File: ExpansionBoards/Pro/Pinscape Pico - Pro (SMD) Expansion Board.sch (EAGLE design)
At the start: 175 parts, among them IC1 UCC27523D, IC10 UCC27523D, IC11 UCC27523D, IC12 UCC27523D, IC13 UCC27523D, IC14 UCC27523D, IC15 TLC59116FIRHBR, IC16 TLC59116FIRHBR, IC17 TLC59116FIRHBR, IC18 TLC59116FIRHBR, IC19 ULN2803ADWR, IC2 UCC27523D, IC20 ULN2803ADWR, IC21 ULN2803ADWR, IC22 ULN2803ADWR, IC23 ULN2803ADWR, IC24 PCA9555APW,118, IC25 PCA9555APW,118, IC26 LIS3DHTR, IC27 SN74LVC1G175DCKR, IC28 APX809S-29SA-7, IC29 LTV-827S, IC3 UCC27523D, IC30 ADS1115IDGSR, IC31 TLV75733PDBVR, IC33 RV-3032-C7, IC4 UCC27523D, IC5 UCC27523D, IC6 UCC27523D, IC7 UCC27523D, IC8 UCC27523D, IC9 UCC27523D, J1 640445-4, J10 1-640456-0, J11 1-640456-0, J12 1-640456-0, J13 640445-5, J14 640445-9, J15 640445-9, J16 640445-9, J18 BM03B-SRSS-TB(LF)(SN), J2 30316-6002HB, J3 1-640456-0, J4 640456-9, J5 640456-9, J6 640454-2, J7 215079-4, J8 30308-6002HB, J9 1-640456-0, Q1 BUK7K89-100EX, Q10 BUK7K89-100EX, Q11 BUK7K89-100EX, Q12 BUK7K89-100EX, Q13 BUK7K89-100EX, Q14 BUK7K89-100EX, Q15 UMA5NTR, Q16 UMA5NTR, Q17 UMA5NTR, Q18 UMA5NTR, Q19 UMA5NTR, Q2 BUK7K89-100EX, Q20 UMA5NTR, Q21 UMA5NTR, Q22 UMA5NTR, Q23 UMA5NTR, Q24 UMA5NTR, Q25 UMA5NTR, Q26 UMA5NTR, Q29 DMG2302UK-7, Q3 BUK7K89-100EX, Q4 BUK7K89-100EX, Q5 BUK7K89-100EX, Q6 BUK7K89-100EX, Q7 BUK7K89-100EX, Q8 BUK7K89-100EX, Q9 BUK7K89-100EX, SW1 TS-1187A-B-A-B, U1 BAT-HLD-001-THM

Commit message: bug fixes
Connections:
- net 3V3_PERIPHERAL: now also IC26.CS
- net GND: now also IC26.SDO/SA0; no longer IC26.CS
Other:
- note added: "CS = VDD -> I2C mode"
- note added: "I2C Addresses Use 7-bit address notation, per Pico SDK conventions $18 LIS3DHTR (accelerometer) $20 IC24 PCA9555 (GPIO expander) $21 IC25 PCA9555 (GPIO expander) $48 IC29 ADS1115 (ADC) $51 IC32 RV-3032-C7 (RTC) $60 IC15 TLC59116F (PWM) $61 IC16 TLC59116F (PWM) $62 IC17 TLC59116F (PWM) $63 IC18 TLC59116F (PWM) Note: TLC59116F addresses $68 and $6B are reserved; do not use for new chips added to th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"
- note added: "SDO/SA0 sets I2C address: GND = 0x18, VDD = 0x19"
- note removed: "I2C Addresses Use 7-bit address notation, per Pico SDK conventions $20 IC24 PCA9555 (GPIO expander) $21 IC25 PCA9555 (GPIO expander) $48 IC29 ADS1115 (ADC) $4C IC15 MC3416 (Accelerometer) $51 IC32 RV-3032-C7 (RTC) $60 IC15 TLC59116F (PWM) $61 IC16 TLC59116F (PWM) $62 IC17 TLC59116F (PWM) $63 IC18 TLC59116F (PWM) Note: TLC59116F addresses $68 and $6B are reserved; do not use for new chips added to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"
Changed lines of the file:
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@@
 <part name="J19" library="pinhead" deviceset="PINHD-1X6" device=""/>
 <part name="IC26" library="SamacSys_Parts" deviceset="LIS3DHTR" device=""/>
-<part name="GND42" library="supply1" deviceset="GND" device=""/>
 <part name="GND51" library="supply1" deviceset="GND" device=""/>
 <part name="GND52" library="supply1" deviceset="GND" device=""/>
@@
 <part name="R49" library="resistor" deviceset="R-US_" device="R0402" value="100R"/>
 <part name="R50" library="resistor" deviceset="R-US_" device="R0402" value="330R"/>
+<part name="GND42" library="supply1" deviceset="GND" device=""/>
 </parts>
 <sheets>
@@
 <plain>
 <text x="73.66" y="68.58" size="2.54" layer="91">Accelerometer</text>
+<text x="81.28" y="-3.048" size="1.778" layer="91" align="center-left">SDO/SA0 sets I2C address:
+GND = 0x18, VDD = 0x19</text>
+<text x="107.95" y="7.874" size="1.778" layer="91" align="center-left">CS = VDD -&gt; I2C mode</text>
 </plain>
 <instances>
@@
 <attribute name="VALUE" x="97.79" y="22.86" size="1.778" layer="96" align="center-left"/>
 </instance>
-<instance part="GND42" gate="1" x="86.36" y="5.08" rot="MR0"/>
 <instance part="GND51" gate="1" x="60.96" y="35.56" rot="MR90"/>
 <instance part="GND52" gate="1" x="106.68" y="38.1" rot="MR270"/>
 <instance part="GND50" gate="1" x="106.68" y="43.18" rot="MR270"/>
+<instance part="GND42" gate="1" x="83.82" y="2.54" rot="MR0"/>
 </instances>
 <busses>
@@
 </segment>
 <segment>
-<pinref part="IC26" gate="G$1" pin="CS"/>
-<pinref part="GND42" gate="1" pin="GND"/>
-<wire x1="86.36" y1="10.16" x2="86.36" y2="7.62" width="0.1524" layer="91"/>
-</segment>
-<segment>
 <pinref part="GND51" gate="1" pin="GND"/>
 <pinref part="IC26" gate="G$1" pin="GND_1"/>
@@
 <pinref part="GND50" gate="1" pin="GND"/>
 </segment>
+<segment>
+<pinref part="IC26" gate="G$1" pin="SDO/SA0"/>
+<wire x1="83.82" y1="10.16" x2="83.82" y2="5.08" width="0.1524" layer="91"/>
+<pinref part="GND42" gate="1" pin="GND"/>
+</segment>
 </net>
 <net name="SDA" class="0">
@@
 <pinref part="IC26" gate="G$1" pin="SDA/SDI/SDO"/>
 <wire x1="81.28" y1="10.16" x2="81.28" y2="7.62" width="0.1524" layer="91"/>
-<label x="81.28" y="7.62" size="1.27" layer="95" rot="R270" xref="yes"/>
+<wire x1="81.28" y1="7.62" x2="78.74" y2="7.62" width="0.1524" layer="91"/>
+<label x="78.74" y="7.62" size="1.27" layer="95" rot="R180" xref="yes"/>
 </segment>
 </net>
@@
 <junction x="43.18" y="45.72"/>
 </segment>
+<segment>
+<wire x1="88.9" y1="7.62" x2="86.36" y2="7.62" width="0.1524" layer="91"/>
+<pinref part="IC26" gate="G$1" pin="CS"/>
+<wire x1="86.36" y1="7.62" x2="86.36" y2="10.16" width="0.1524" layer="91"/>
+<label x="88.9" y="7.62" size="1.27" layer="95" xref="yes"/>
+</segment>
 </net>
 </nets>
@@
 Use 7-bit address notation, per
 Pico SDK conventions
+  $18  LIS3DHTR (accelerometer)
   $20  IC24 PCA9555 (GPIO expander)
   $21  IC25 PCA9555 (GPIO expander)
   $48  IC29 ADS1115 (ADC)
-  $4C  IC15 MC3416 (Accelerometer)
   $51  IC32 RV-3032-C7 (RTC)
   $60  IC15 TLC59116F (PWM)

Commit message: expansion board improvements
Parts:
- J1: value 640445-4 -> 640445-6; device SamacSys_Parts:640445-4 -> SamacSys_Parts:640445-6
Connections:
- net 12V: now also J1.5; no longer J1.4
- net 5V: now also J1.6; no longer J1.1
- net GND: now also J1.1, J1.4
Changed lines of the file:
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@@
 <part name="J11" library="SamacSys_Parts" deviceset="1-640456-0" device=""/>
 <part name="J12" library="SamacSys_Parts" deviceset="1-640456-0" device=""/>
-<part name="J1" library="SamacSys_Parts" deviceset="640445-4" device=""/>
 <part name="J7" library="SamacSys_Parts" deviceset="215079-4" device=""/>
 <part name="GND7" library="supply1" deviceset="GND" device=""/>
@@
 <part name="R50" library="resistor" deviceset="R-US_" device="R0402" value="330R"/>
 <part name="GND42" library="supply1" deviceset="GND" device=""/>
+<part name="J1" library="SamacSys_Parts" deviceset="640445-6" device=""/>
 </parts>
 <sheets>
@@
 <attribute name="NAME" x="99.06" y="78.74" size="2.54" layer="95" align="center"/>
 </instance>
-<instance part="GND1" gate="1" x="25.4" y="119.38" rot="R270"/>
+<instance part="GND1" gate="1" x="38.1" y="121.92" rot="R270"/>
 <instance part="R41" gate="G$1" x="205.74" y="50.8" smashed="yes" rot="R90">
 <attribute name="NAME" x="207.264" y="51.2826" size="1.778" layer="95"/>
@@
 <attribute name="NAME" x="104.648" y="121.3866" size="1.778" layer="95"/>
 <attribute name="VALUE" x="110.49" y="121.412" size="1.778" layer="96"/>
-</instance>
-<instance part="J1" gate="G$1" x="45.72" y="121.92" smashed="yes">
-<attribute name="NAME" x="61.722" y="122.936" size="1.778" layer="95" align="center-left"/>
-<attribute name="VALUE" x="61.722" y="120.396" size="1.778" layer="96" align="center-left"/>
 </instance>
 <instance part="J18" gate="A" x="208.28" y="116.84" smashed="yes">
@@
 </instance>
 <instance part="GND49" gate="1" x="314.96" y="12.7"/>
+<instance part="J1" gate="G$1" x="45.72" y="121.92" smashed="yes">
+<attribute name="NAME" x="62.23" y="121.92" size="1.778" layer="95" align="center-left"/>
+<attribute name="VALUE" x="62.23" y="119.38" size="1.778" layer="96" align="center-left"/>
+</instance>
 </instances>
 <busses>
@@
 <net name="GND" class="0">
 <segment>
-<wire x1="45.72" y1="119.38" x2="30.48" y2="119.38" width="0.1524" layer="91"/>
-<wire x1="45.72" y1="116.84" x2="30.48" y2="116.84" width="0.1524" layer="91"/>
-<wire x1="30.48" y1="116.84" x2="30.48" y2="119.38" width="0.1524" layer="91"/>
-<wire x1="30.48" y1="119.38" x2="27.94" y2="119.38" width="0.1524" layer="91"/>
+<wire x1="45.72" y1="116.84" x2="43.18" y2="116.84" width="0.1524" layer="91"/>
+<wire x1="43.18" y1="116.84" x2="43.18" y2="119.38" width="0.1524" layer="91"/>
+<wire x1="43.18" y1="119.38" x2="43.18" y2="121.92" width="0.1524" layer="91"/>
+<wire x1="43.18" y1="121.92" x2="40.64" y2="121.92" width="0.1524" layer="91"/>
 <pinref part="GND1" gate="1" pin="GND"/>
-<junction x="30.48" y="119.38"/>
+<junction x="43.18" y="121.92"/>
+<wire x1="43.18" y1="116.84" x2="43.18" y2="114.3" width="0.1524" layer="91"/>
+<junction x="43.18" y="116.84"/>
+<wire x1="43.18" y1="114.3" x2="45.72" y2="114.3" width="0.1524" layer="91"/>
 <pinref part="J1" gate="G$1" pin="2"/>
 <pinref part="J1" gate="G$1" pin="3"/>
+<pinref part="J1" gate="G$1" pin="4"/>
+<wire x1="45.72" y1="119.38" x2="43.18" y2="119.38" width="0.1524" layer="91"/>
+<junction x="43.18" y="119.38"/>
+<pinref part="J1" gate="G$1" pin="1"/>
+<wire x1="43.18" y1="121.92" x2="45.72" y2="121.92" width="0.1524" layer="91"/>
 </segment>
 <segment>
@@
 <net name="5V" class="0">
 <segment>
-<label x="43.18" y="121.92" size="1.27" layer="95" rot="R180" xref="yes"/>
-<pinref part="J1" gate="G$1" pin="1"/>
-<wire x1="43.18" y1="121.92" x2="45.72" y2="121.92" width="0.1524" layer="91"/>
+<label x="43.18" y="109.22" size="1.27" layer="95" rot="R180" xref="yes"/>
+<pinref part="J1" gate="G$1" pin="6"/>
+<wire x1="45.72" y1="109.22" x2="43.18" y2="109.22" width="0.1524" layer="91"/>
 </segment>
 </net>
@@
 <net name="12V" class="0">
 <segment>
-<label x="43.18" y="114.3" size="1.27" layer="95" rot="R180" xref="yes"/>
-<pinref part="J1" gate="G$1" pin="4"/>
-<wire x1="43.18" y1="114.3" x2="45.72" y2="114.3" width="0.1524" layer="91"/>
-</segment>
-</net>
+<label x="43.18" y="111.76" size="1.27" layer="95" rot="R180" xref="yes"/>
+<pinref part="J1" gate="G$1" pin="5"/>
+<wire x1="45.72" y1="111.76" x2="43.18" y2="111.76" width="0.1524" layer="91"/>
+</segment>
+</net>

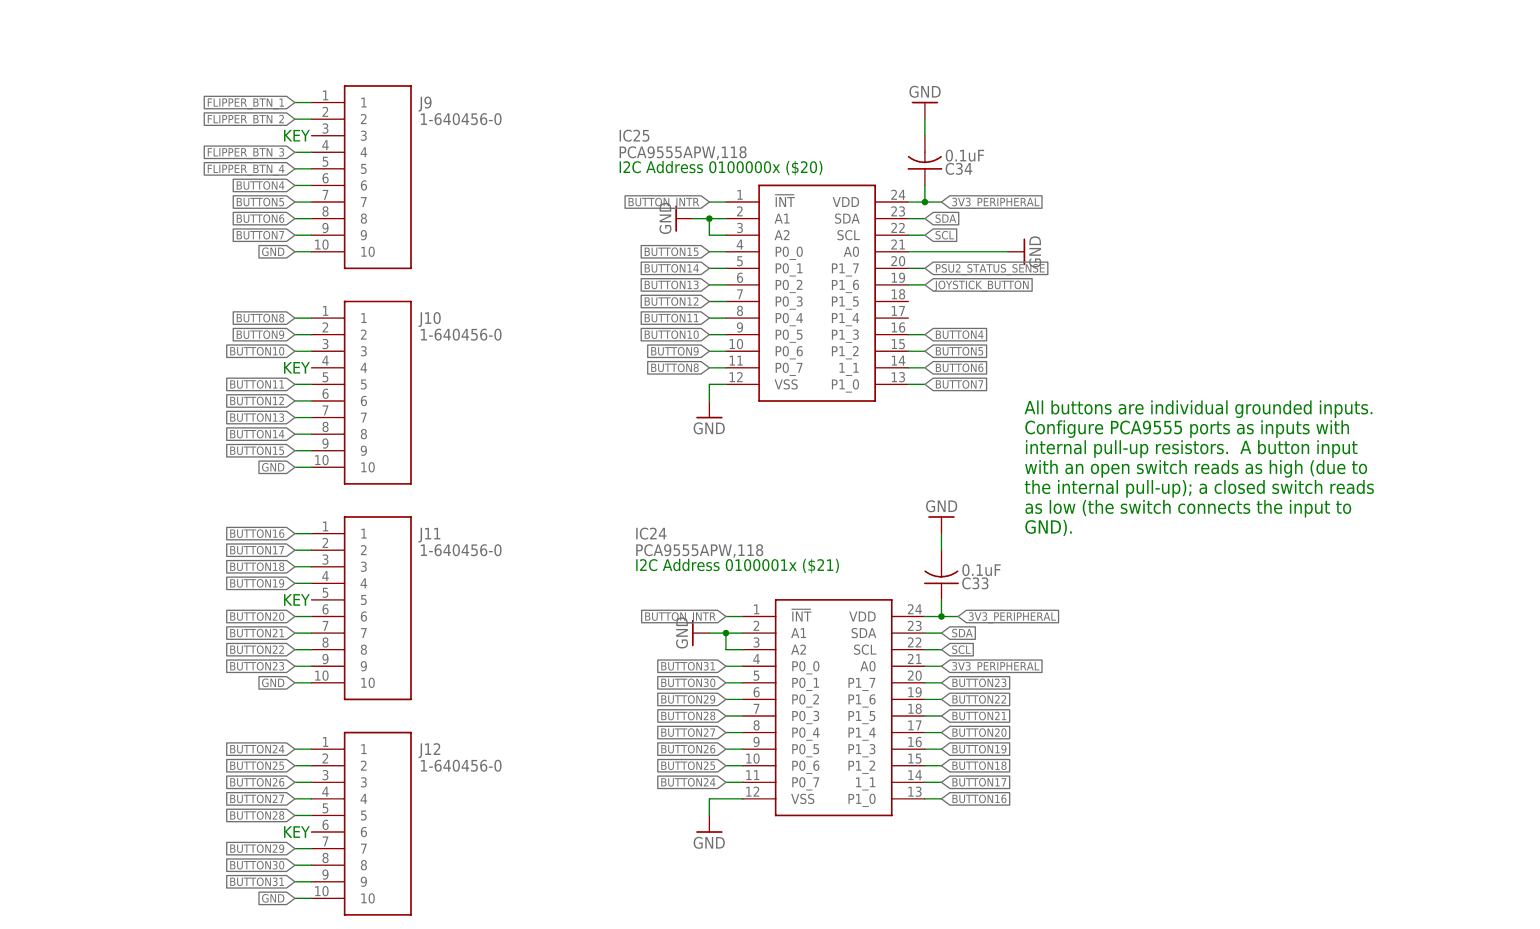
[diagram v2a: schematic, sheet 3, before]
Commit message: Update Pro expansion board to use 74HC165 for all button inputs
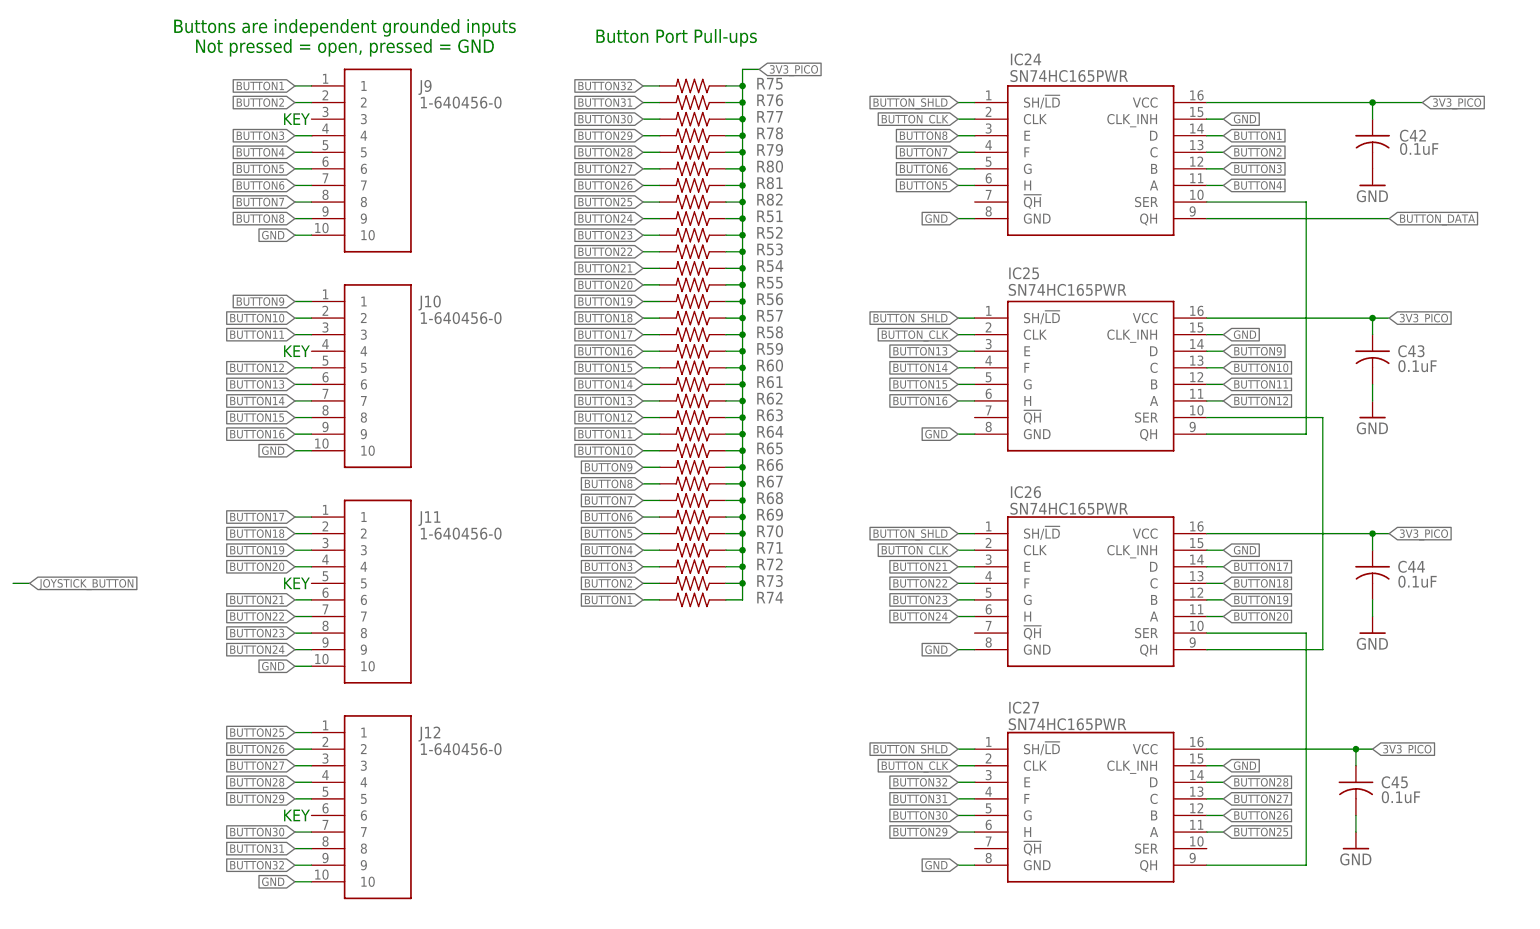
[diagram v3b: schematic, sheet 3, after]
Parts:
- removed C33, C34: 0.1uF, rcl:C-USC0402
- added C42, C43, C44, C45: 0.1uF, rcl:C-USC0402
- added IC32: ADS1115IDGSR, SamacSys_Parts:ADS1115IDGSR
- added IC34: RV-3032-C7, SamacSys_Parts:RV-3032-C7_32.768KHZ-2.5PPM-TA
- added R51, R52, R53, R54, R55, R56, R57, R58, R59, R60, R61, R62, R63, R64, R65, R66, R67, R68, R69, R70, R71, R72, R73, R74, R75, R76, R77, R78, R79, R80, R81, R82: 10k, resistor:R-US_R0402
- IC24, IC25: value PCA9555APW,118 -> SN74HC165PWR; device SamacSys_Parts:PCA9555APW,118 -> SamacSys_Parts:SN74HC165PWR
- IC26: value LIS3DHTR -> SN74HC165PWR; device SamacSys_Parts:LIS3DHTR -> SamacSys_Parts:SN74HC165PWR
- IC27: value SN74LVC1G175DCKR -> SN74HC165PWR; device SamacSys_Parts:SN74LVC1G175DCKR -> SamacSys_Parts:SN74HC165PWR
- IC28: value APX809S-29SA-7 -> LIS3DHTR; device SamacSys_Parts:APX809S-40SA-7 -> SamacSys_Parts:LIS3DHTR; MANUFACTURER_PART_NUMBER APX809S-40SA-7 -> (none)
- IC29: value LTV-827S -> SN74LVC1G175DCKR; device SamacSys_Parts:LTV-827S -> SamacSys_Parts:SN74LVC1G175DCKR
- IC30: value ADS1115IDGSR -> APX809S-29SA-7; device SamacSys_Parts:ADS1115IDGSR -> SamacSys_Parts:APX809S-40SA-7; MANUFACTURER_PART_NUMBER (none) -> APX809S-40SA-7
- IC31: value TLV75733PDBVR -> LTV-827S; device SamacSys_Parts:TLV75733PDBVR -> SamacSys_Parts:LTV-827S
- IC33: value RV-3032-C7 -> TLV75733PDBVR; device SamacSys_Parts:RV-3032-C7_32.768KHZ-2.5PPM-TA -> SamacSys_Parts:TLV75733PDBVR
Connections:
- removed net BUTTON_INTR: IC24.!INT, IC25.!INT, PICO1.GP19
- removed net FLIPPER_BTN_1: J9.1, PICO1.GP27_A1
- removed net FLIPPER_BTN_2: J9.2, PICO1.GP26_A0
- removed net FLIPPER_BTN_3: J9.4, PICO1.GP22
- removed net FLIPPER_BTN_4: J9.5, PICO1.GP21
- new net BUTTON1: IC24.D, J9.1, R74.2
- new net BUTTON2: IC24.C, J9.2, R73.2
- new net BUTTON3: IC24.B, J9.4, R72.2
- new net BUTTON32: IC27.E, J12.9, R75.2
- new net BUTTON_CLK: IC24.CLK, IC25.CLK, IC26.CLK, IC27.CLK, PICO1.GP21
- new net BUTTON_DATA: IC24.QH, PICO1.GP26_A0
- new net BUTTON_SHLD: IC24.SH/!LD, IC25.SH/!LD, IC26.SH/!LD, IC27.SH/!LD, PICO1.GP22
- new net N$78: IC25.SER, IC26.QH
- new net N$79: IC24.SER, IC25.QH
- new net N$80: IC26.SER, IC27.QH
- net 3V3_PERIPHERAL: now also IC28.CS, IC28.VDD, IC28.VDDIO, IC31.C_1, IC32.VDD, IC33.OUT, IC34.VDD; no longer C33.1, C34.1, IC24.A0, IC24.VDD, IC25.VDD, IC26.CS, IC26.VDD, IC26.VDDIO, IC29.C_1, IC30.VDD, IC31.OUT, IC33.VDD
- net 3V3_PERIPHERAL_ENABLE: now also IC33.EN; no longer IC31.EN
- net 3V3_PICO: now also C42.1, C43.1, C44.1, C45.1, IC24.VCC, IC25.VCC, IC26.VCC, IC27.VCC, R51.1, R52.1, R53.1, R54.1, R55.1, R56.1, R57.1, R58.1, R59.1, R60.1, R61.1, R62.1, R63.1, R64.1, R65.1, R66.1, R67.1, R68.1, R69.1, R70.1, R71.1, R72.1, R73.1, R74.1, R75.1, R76.1, R77.1, R78.1, R79.1, R80.1, R81.1, R82.1
- net 5V: now also IC29.D, IC29.VCC, IC30.VCC, IC31.C_2; no longer IC27.D, IC27.VCC, IC28.VCC, IC29.C_2
- net ACCEL_INTR: now also IC28.INT1; no longer IC26.INT1
- net ADC_INTR: now also IC32.ALERT/RDY; no longer IC30.ALERT/RDY
- net BUTTON10: now also IC25.C, J10.2, R65.2; no longer IC25.P0_5, J10.3
- net BUTTON11: now also IC25.B, J10.3, R64.2; no longer IC25.P0_4, J10.5
- net BUTTON12: now also IC25.A, J10.5, R63.2; no longer IC25.P0_3, J10.6
- net BUTTON13: now also IC25.E, J10.6, R62.2; no longer IC25.P0_2, J10.7
- net BUTTON14: now also IC25.F, J10.7, R61.2; no longer IC25.P0_1, J10.8
- net BUTTON15: now also IC25.G, J10.8, R60.2; no longer IC25.P0_0, J10.9
- net BUTTON16: now also IC25.H, J10.9, R59.2; no longer IC24.P1_0, J11.1
- net BUTTON17: now also IC26.D, J11.1, R58.2; no longer IC24.1_1, J11.2
- net BUTTON18: now also IC26.C, J11.2, R57.2; no longer IC24.P1_2, J11.3
- net BUTTON19: now also IC26.B, J11.3, R56.2; no longer IC24.P1_3, J11.4
- net BUTTON20: now also IC26.A, J11.4, R55.2; no longer IC24.P1_4, J11.6
- net BUTTON21: now also IC26.E, J11.6, R54.2; no longer IC24.P1_5, J11.7
- net BUTTON22: now also IC26.F, J11.7, R53.2; no longer IC24.P1_6, J11.8
- net BUTTON23: now also IC26.G, J11.8, R52.2; no longer IC24.P1_7, J11.9
- net BUTTON24: now also IC26.H, J11.9, R51.2; no longer IC24.P0_7, J12.1
- net BUTTON25: now also IC27.A, J12.1, R82.2; no longer IC24.P0_6, J12.2
- net BUTTON26: now also IC27.B, J12.2, R81.2; no longer IC24.P0_5, J12.3
- net BUTTON27: now also IC27.C, J12.3, R80.2; no longer IC24.P0_4, J12.4
- net BUTTON28: now also IC27.D, J12.4, R79.2; no longer IC24.P0_3, J12.5
- net BUTTON29: now also IC27.H, J12.5, R78.2; no longer IC24.P0_2, J12.7
- net BUTTON30: now also IC27.G, J12.7, R77.2; no longer IC24.P0_1, J12.8
- net BUTTON31: now also IC27.F, J12.8, R76.2; no longer IC24.P0_0, J12.9
- net BUTTON4: now also IC24.A, J9.5, R71.2; no longer IC25.P1_3, J9.6
- net BUTTON5: now also IC24.H, J9.6, R70.2; no longer IC25.P1_2, J9.7
- net BUTTON6: now also IC24.G, J9.7, R69.2; no longer IC25.1_1, J9.8
- net BUTTON7: now also IC24.F, J9.8, R68.2; no longer IC25.P1_0, J9.9
- net BUTTON8: now also IC24.E, J9.9, R67.2; no longer IC25.P0_7, J10.1
- net BUTTON9: now also IC25.D, J10.1, R66.2; no longer IC25.P0_6, J10.2
- net GND: now also C42.2, C43.2, C44.2, C45.2, IC24.CLK_INH, IC24.GND, IC25.CLK_INH, IC25.GND, IC26.CLK_INH, IC26.GND, IC27.CLK_INH, IC28.GND_1, IC28.GND_2, IC28.RES, IC28.SDO/SA0, IC29.GND, IC32.ADDR, IC32.GND, IC33.GND, IC34.VSS; no longer C33.2, C34.2, IC24.A1, IC24.A2, IC24.VSS, IC25.A0, IC25.A1, IC25.A2, IC25.VSS, IC26.GND_1, IC26.GND_2, IC26.RES, IC26.SDO/SA0, IC28.GND, IC30.ADDR, IC31.GND, IC33.VSS
- net JOYSTICK_BUTTON: now also PICO1.GP27_A1; no longer IC25.P1_6
- net JOYSTICK_X: now also IC32.AIN2; no longer IC30.AIN2
- net JOYSTICK_Y: now also IC32.AIN1; no longer IC30.AIN1
- net N$58: now also IC29.CLK, IC31.E_2; no longer IC27.CLK, IC29.E_2
- net N$59: now also IC31.K_1; no longer IC29.K_1
- net N$63: now also IC29.!CLR, IC30.!RESET; no longer IC27.!CLR, IC28.!RESET
- net N$65: now also IC31.K_2; no longer IC29.K_2
- net N$68: now also IC29.Q, IC31.A_2; no longer IC27.Q, IC29.A_2
- net N$71: now also IC32.AIN3; no longer IC30.AIN3
- net N$73: now also IC34.EVI; no longer IC33.EVI
- net N$76: now also IC34.VBACKUP; no longer IC33.VBACKUP
- net PLUNGER_ADC: now also IC32.AIN0; no longer IC30.AIN0
- net PSU2_STATUS_SENSE: now also IC31.E_1, PICO1.GP19; no longer IC25.P1_7, IC29.E_1
- net PSU2_STATUS_SET: now also IC31.A_1; no longer IC29.A_1
- net SCL: now also IC28.SCL/SPC, IC32.SCL, IC34.SCL; no longer IC24.SCL, IC25.SCL, IC26.SCL/SPC, IC30.SCL, IC33.SCL
- net SDA: now also IC28.SDA/SDI/SDO, IC32.SDA, IC34.SDA; no longer IC24.SDA, IC25.SDA, IC26.SDA/SDI/SDO, IC30.SDA, IC33.SDA
- net VBUS: now also IC33.IN; no longer IC31.IN
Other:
- note added: "Button Port Pull-ups"
- note added: "Buttons are independent grounded inputs Not pressed = open, pressed = GND"
- note added: "I2C Addresses Use 7-bit address notation, per Pico SDK conventions $18 LIS3DHTR (accelerometer) $48 IC29 ADS1115 (ADC) $51 IC32 RV-3032-C7 (RTC) $60 IC15 TLC59116F (PWM) $61 IC16 TLC59116F (PWM) $62 IC17 TLC59116F (PWM) $63 IC18 TLC59116F (PWM) Note: TLC59116F addresses $68 and $6B are reserved; do not use for new chips added to the design."
- note removed: "All buttons are individual grounded inputs. Configure PCA9555 ports as inputs with internal pull-up resistors. A button input with an open switch reads as high (due to the internal pull-up); a closed switch reads as low (the switch connects the input to GND)."
- note removed: "I2C Address 0100000x ($20)"
- note removed: "I2C Address 0100001x ($21)"
- note removed: "I2C Addresses Use 7-bit address notation, per Pico SDK conventions $18 LIS3DHTR (accelerometer) $20 IC24 PCA9555 (GPIO expander) $21 IC25 PCA9555 (GPIO expander) $48 IC29 ADS1115 (ADC) $51 IC32 RV-3032-C7 (RTC) $60 IC15 TLC59116F (PWM) $61 IC16 TLC59116F (PWM) $62 IC17 TLC59116F (PWM) $63 IC18 TLC59116F (PWM) Note: TLC59116F addresses $68 and $6B are reserved; do not use for new chips added to th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"
- moved on the sheet: J10, J11, J12, J9
